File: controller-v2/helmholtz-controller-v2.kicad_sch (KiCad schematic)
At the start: 25 parts, among them U1 BDS63150AFM, U2 BDS63150AFM, U3 INA226, U4 INA226, U5 BDS63150AFM, U6 INA226, U7 RPi_Pico

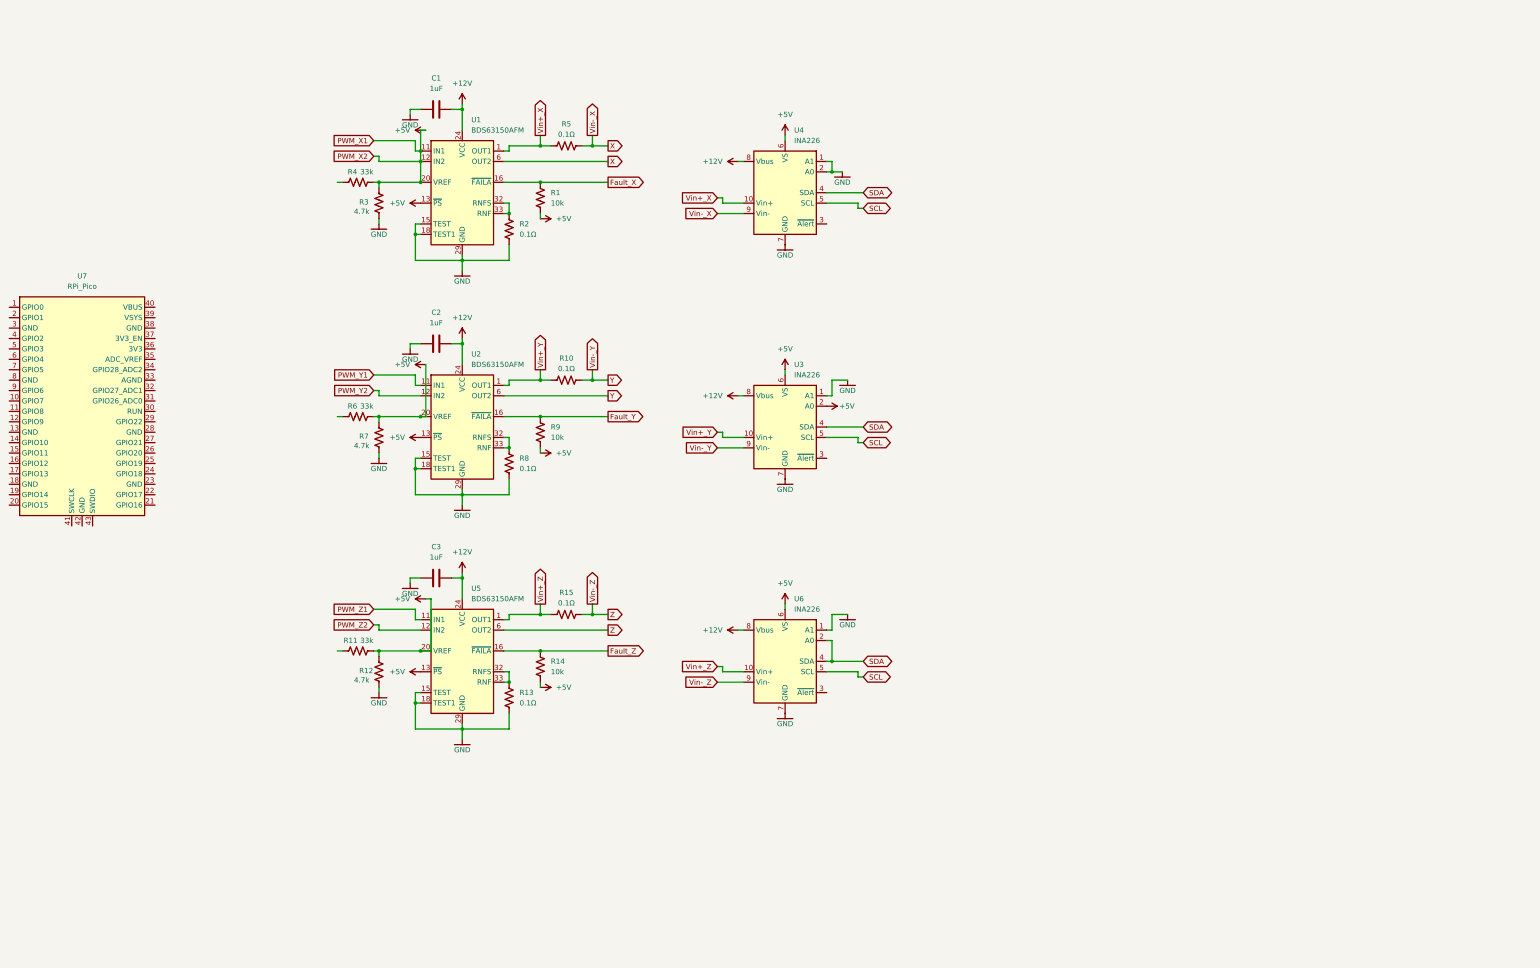
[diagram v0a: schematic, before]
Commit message: Improved schematic, made it more readable
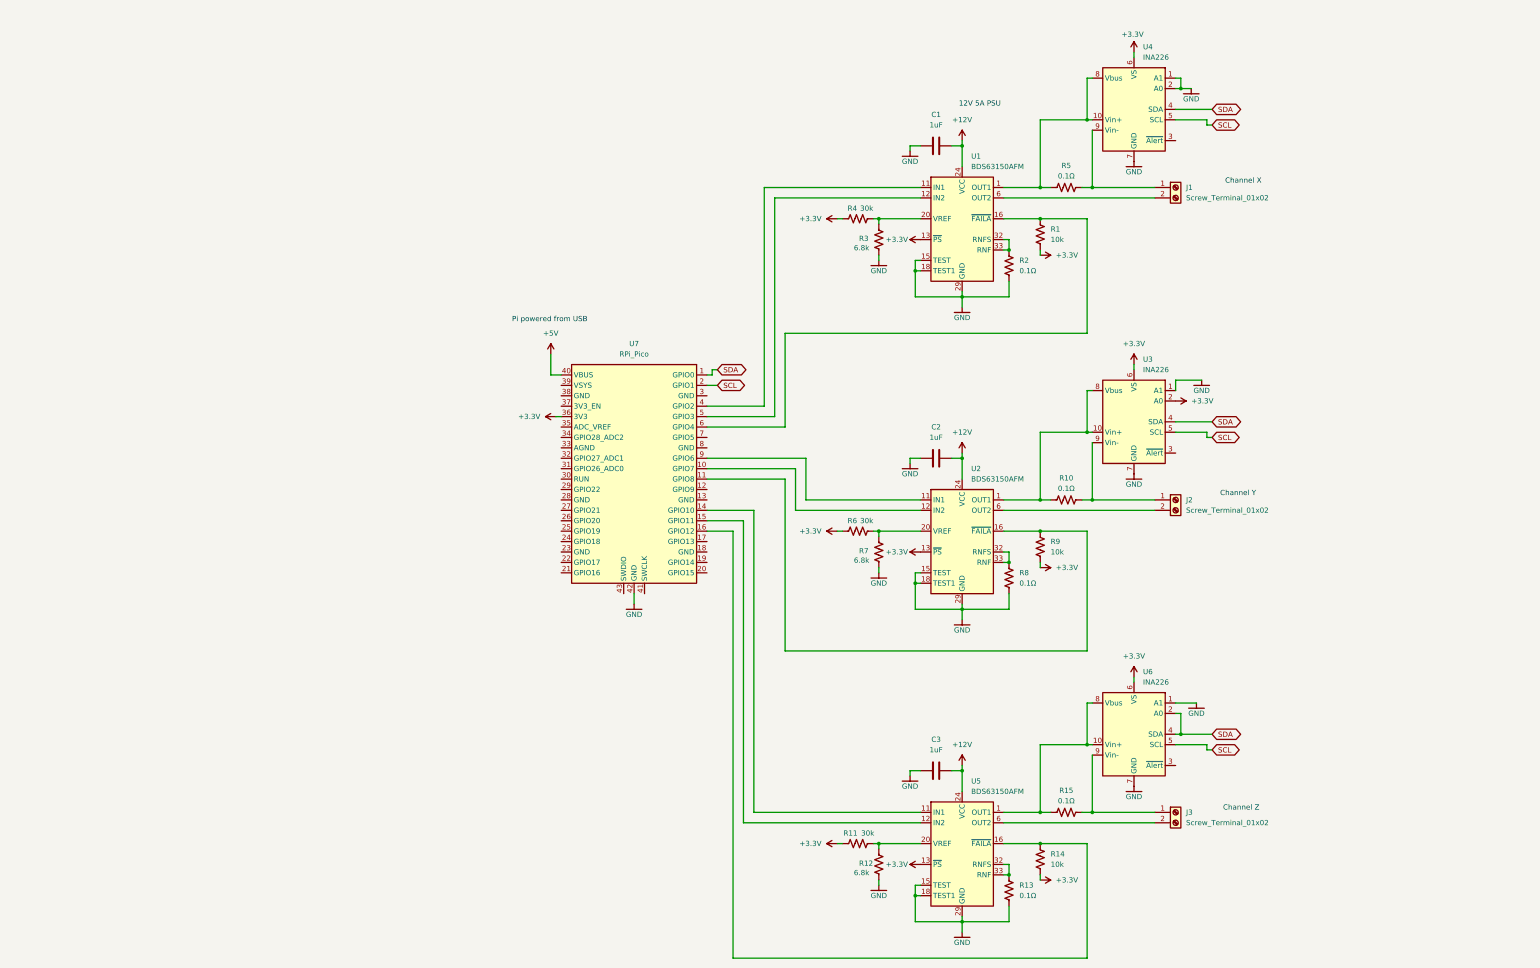
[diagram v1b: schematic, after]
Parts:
- added J1, J2, J3: Screw_Terminal_01x02, symbol Connector:Screw_Terminal_01x02
- R11, R4, R6: value 33k -> 30k
- R12, R3, R7: value 4.7k -> 6.8k
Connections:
- net Fault_X is gone; now on an unnamed net: R1.1, U1.16 (~{FAILA})
- net Fault_Y is gone; now on an unnamed net: R9.1, U2.16 (~{FAILA})
- net Fault_Z is gone; now on an unnamed net: R14.1, U5.16 (~{FAILA})
- net PWM_Y1 is gone; now on an unnamed net: U2.11 (IN1)
- net PWM_Y2 is gone; now on an unnamed net: U2.12 (IN2)
- net PWM_Z1 is gone; now on an unnamed net: U5.11 (IN1)
- net PWM_Z2 is gone; now on an unnamed net: U5.12 (IN2)
- net +12V: no longer U3.8 (Vbus), U4.8 (Vbus), U6.8 (Vbus)
- net +5V: now also U7.40 (VBUS); no longer R1.2, R11.2, R12.2, R14.2, R3.2, R4.2, R6.2, R7.2, R9.2, U1.11 (IN1), U1.12 (IN2), U1.13 (~{PS}), U1.20 (VREF), U2.13 (~{PS}), U2.20 (VREF), U3.2 (A0), U3.6 (VS), U4.6 (VS), U5.13 (~{PS}), U5.20 (VREF), U6.6 (VS)
- net GND: now also U7.42 (GND)
- net SCL: now also U7.2 (GPIO1)
- net SDA: now also U7.1 (GPIO0)
- net +3.3V: now reaches U7.36 (3V3)
- net +3.3V: now also R1.2, R11.1, R14.2, R4.1, R6.1, R9.2, U1.13 (~{PS}), U2.13 (~{PS}), U3.2 (A0), U3.6 (VS), U4.6 (VS), U5.13 (~{PS}), U6.6 (VS)
- net at U7.4 (GPIO2): now also U1.11 (IN1)
- net at U7.5 (GPIO3): now also U1.12 (IN2)
- net Vin+_X: no longer names the net of R5.1, U1.1 (OUT1), U1.2 (OUT1), U1.3 (OUT1), U4.10 (Vin+)
- net Vin+_X: now also U4.8 (Vbus)
- net Vin+_Y: no longer names the net of R10.1, U2.1 (OUT1), U2.2 (OUT1), U2.3 (OUT1), U3.10 (Vin+)
- net Vin+_Y: now also U3.8 (Vbus)
- net Vin+_Z: no longer names the net of R15.1, U5.1 (OUT1), U5.2 (OUT1), U5.3 (OUT1), U6.10 (Vin+)
- net Vin+_Z: now also U6.8 (Vbus)
- net Vin-_X: no longer names the net of U1.6 (OUT2), U1.7 (OUT2), U1.8 (OUT2)
- net Vin-_X: now also J1.2 (Pin_2); no longer R5.2, U4.9 (Vin-)
- net Vin-_Y: no longer names the net of U2.6 (OUT2), U2.7 (OUT2), U2.8 (OUT2)
- net Vin-_Y: now also J2.2 (Pin_2); no longer R10.2, U3.9 (Vin-)
- net Vin-_Z: no longer names the net of U5.6 (OUT2), U5.7 (OUT2), U5.8 (OUT2)
- net Vin-_Z: now also J3.2 (Pin_2); no longer R15.2, U6.9 (Vin-)
- new net: R6.2, R7.2, U2.20 (VREF)
- new net: J2.1 (Pin_1), R10.2, U3.9 (Vin-)
- new net: R11.2, R12.2, U5.20 (VREF)
- new net: J1.1 (Pin_1), R5.2, U4.9 (Vin-)
- new net: J3.1 (Pin_1), R15.2, U6.9 (Vin-)
- new net: R3.2, R4.2, U1.20 (VREF)
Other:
- note added: "12V 5A PSU"
- note added: "Channel X"
- note added: "Channel Y"
- note added: "Channel Z"
- note added: "Pi powered from USB"
- title: (none) -> Helmholtz Cage Controller
- moved on the sheet: C1, R1, R2, R3, R4, R5, U1, U4, U7

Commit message: ADded 12V connector and I2C resistors
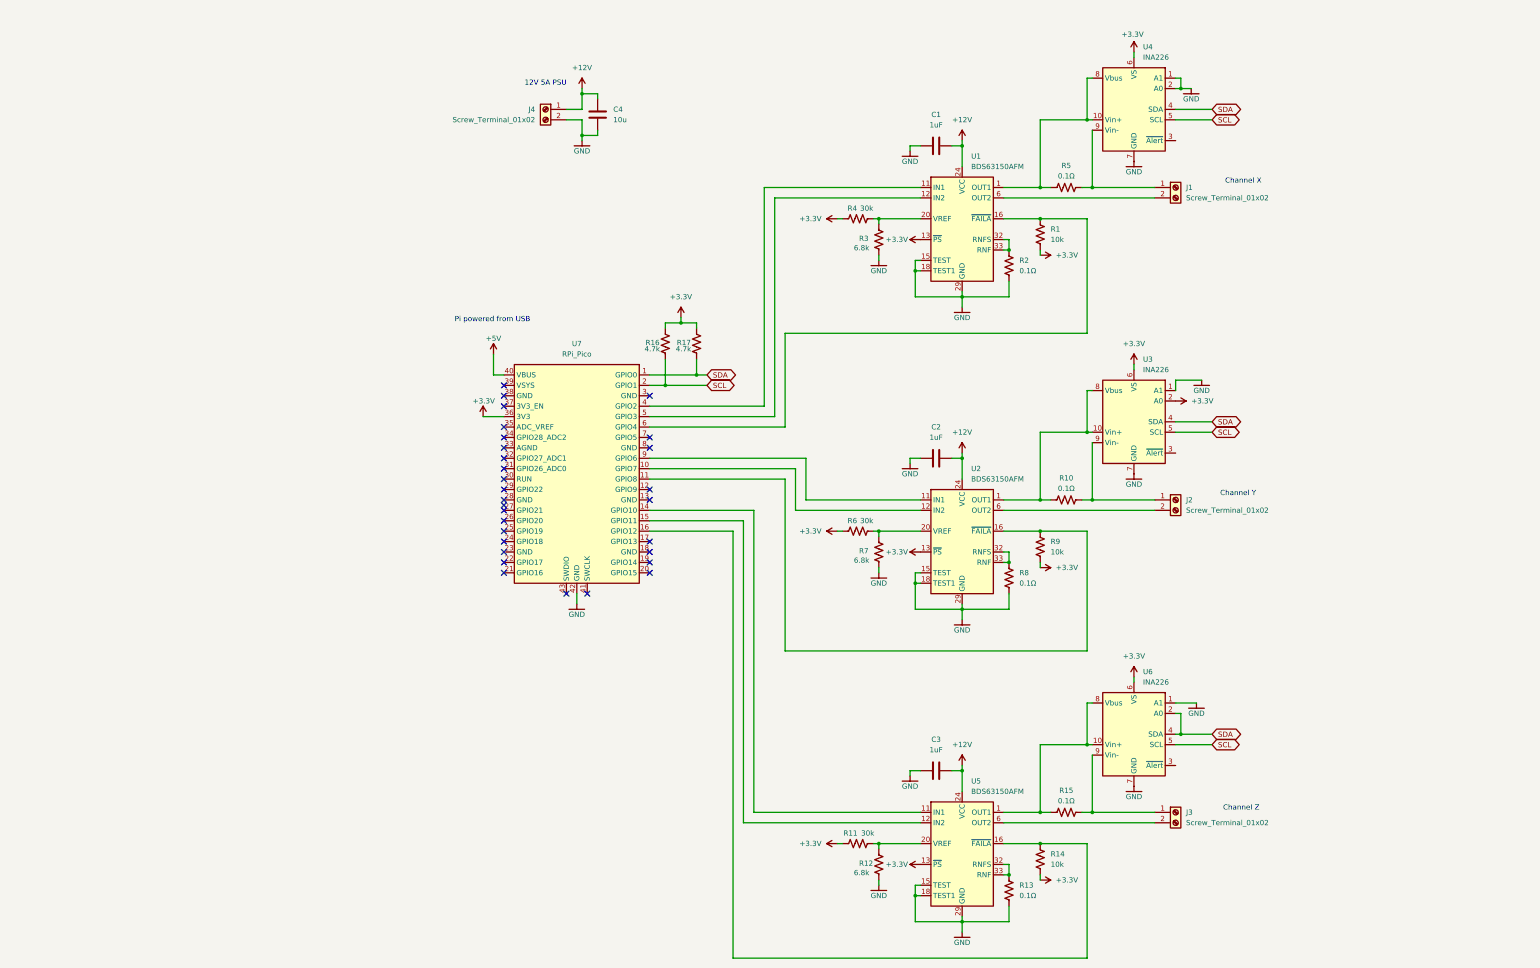
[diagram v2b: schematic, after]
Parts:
- added C4: 10u, symbol Device:C
- added J4: Screw_Terminal_01x02, symbol Connector:Screw_Terminal_01x02
- added R16, R17: 4.7k, symbol Device:R_US
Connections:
- net +12V: now also C4.2, J4.1 (Pin_1)
- net +3.3V: now also R16.2, R17.2
- net GND: now also C4.1, J4.2 (Pin_2)
- net SCL: now also R16.1
- net SDA: now also R17.1
- no-connect marks 0 -> 30
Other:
- moved on the sheet: U7

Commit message: updated schematic
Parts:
- C1, C2, C3, C4: footprint (none) -> Capacitor_SMD:C_0805_2012Metric
- J1, J2, J3, J4: footprint (none) -> TerminalBlock_Phoenix:TerminalBlock_Phoenix_PT-1,5-4-3.5-H_1x04_P3.50mm_Horizontal
- R1, R11, R12, R14, R16, R17, R3, R4, R6, R7, R9: footprint (none) -> Resistor_SMD:R_0603_1608Metric
- R10, R13, R15, R2, R5, R8: footprint (none) -> Resistor_SMD:R_1206_3216Metric
- U1, U2, U5: footprint (none) -> psas-footprints:U-BD63150AFM
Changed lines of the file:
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@@
 			)
 		)
-		(property "Footprint" ""
+		(property "Footprint" "Resistor_SMD:R_1206_3216Metric"
 			(at 234.696 155.194 90)
 			(effects
@@
 			)
 		)
-		(property "Footprint" ""
+		(property "Footprint" "Resistor_SMD:R_0603_1608Metric"
 			(at 197.104 142.494 90)
 			(effects
@@
 			)
 		)
-		(property "Footprint" ""
+		(property "Footprint" "Resistor_SMD:R_0603_1608Metric"
 			(at 156.464 97.536 90)
 			(effects
@@
 			)
 		)
-		(property "Footprint" ""
+		(property "Footprint" "psas-footprints:U-BD63150AFM"
 			(at 222.25 125.73 0)
 			(effects
@@
 			)
 		)
-		(property "Footprint" ""
+		(property "Footprint" "Capacitor_SMD:C_0805_2012Metric"
 			(at 219.71 124.7648 0)
 			(effects
@@
 			)
 		)
-		(property "Footprint" ""
+		(property "Footprint" "Resistor_SMD:R_0603_1608Metric"
 			(at 242.316 223.774 90)
 			(effects
@@
 			)
 		)
-		(property "Footprint" ""
+		(property "Footprint" "psas-footprints:U-BD63150AFM"
 			(at 222.25 201.93 0)
 			(effects
@@
 			)
 		)
-		(property "Footprint" ""
+		(property "Footprint" "TerminalBlock_Phoenix:TerminalBlock_Phoenix_PT-1,5-4-3.5-H_1x04_P3.50mm_Horizontal"
 			(at 274.32 59.69 0)
 			(effects
@@
 			)
 		)
-		(property "Footprint" ""
+		(property "Footprint" "Resistor_SMD:R_0603_1608Metric"
 			(at 200.914 224.536 90)
 			(effects
@@
 			)
 		)
-		(property "Footprint" ""
+		(property "Footprint" "Capacitor_SMD:C_0805_2012Metric"
 			(at 219.71 48.5648 0)
 			(effects
@@
 			)
 		)
-		(property "Footprint" ""
+		(property "Footprint" "TerminalBlock_Phoenix:TerminalBlock_Phoenix_PT-1,5-4-3.5-H_1x04_P3.50mm_Horizontal"
 			(at 274.32 212.09 0)
 			(effects
@@
 			)
 		)
-		(property "Footprint" ""
+		(property "Footprint" "Resistor_SMD:R_1206_3216Metric"
 			(at 234.696 78.994 90)
 			(effects
@@
 			)
 		)
-		(property "Footprint" ""
+		(property "Footprint" "Capacitor_SMD:C_0805_2012Metric"
 			(at 132.3848 38.1 0)
 			(effects
@@
 			)
 		)
-		(property "Footprint" ""
+		(property "Footprint" "Resistor_SMD:R_0603_1608Metric"
 			(at 242.316 71.374 90)
 			(effects
@@
 			)
 		)
-		(property "Footprint" ""
+		(property "Footprint" "TerminalBlock_Phoenix:TerminalBlock_Phoenix_PT-1,5-4-3.5-H_1x04_P3.50mm_Horizontal"
 			(at 120.65 40.64 0)
 			(effects
@@
 			)
 		)
-		(property "Footprint" ""
+		(property "Footprint" "Resistor_SMD:R_1206_3216Metric"
 			(at 234.696 231.394 90)
 			(effects
@@
 			)
 		)
-		(property "Footprint" ""
+		(property "Footprint" "Resistor_SMD:R_0603_1608Metric"
 			(at 242.316 147.574 90)
 			(effects
@@
 			)
 		)
-		(property "Footprint" ""
+		(property "Footprint" "Resistor_SMD:R_1206_3216Metric"
 			(at 247.904 58.674 90)
 			(effects
@@
 			)
 		)
-		(property "Footprint" ""
+		(property "Footprint" "Resistor_SMD:R_0603_1608Metric"
 			(at 197.104 218.694 90)
 			(effects
@@
 			)
 		)
-		(property "Footprint" ""
+		(property "Footprint" "Resistor_SMD:R_1206_3216Metric"
 			(at 247.904 211.074 90)
 			(effects
@@
 			)
 		)
-		(property "Footprint" ""
+		(property "Footprint" "TerminalBlock_Phoenix:TerminalBlock_Phoenix_PT-1,5-4-3.5-H_1x04_P3.50mm_Horizontal"
 			(at 274.32 135.89 0)
 			(effects
@@
 			)
 		)
-		(property "Footprint" ""
+		(property "Footprint" "Capacitor_SMD:C_0805_2012Metric"
 			(at 219.71 200.9648 0)
 			(effects
@@
 			)
 		)
-		(property "Footprint" ""
+		(property "Footprint" "Resistor_SMD:R_0603_1608Metric"
 			(at 200.914 148.336 90)
 			(effects
@@
 			)
 		)
-		(property "Footprint" ""
+		(property "Footprint" "Resistor_SMD:R_0603_1608Metric"
 			(at 197.104 66.294 90)
 			(effects
@@
 			)
 		)
-		(property "Footprint" ""
+		(property "Footprint" "psas-footprints:U-BD63150AFM"
 			(at 222.25 49.53 0)
 			(effects
@@
 			)
 		)
-		(property "Footprint" ""
+		(property "Footprint" "Resistor_SMD:R_0603_1608Metric"
 			(at 200.914 72.136 90)
 			(effects
@@
 			)
 		)
-		(property "Footprint" ""
+		(property "Footprint" "Resistor_SMD:R_1206_3216Metric"
 			(at 247.904 134.874 90)
 			(effects
@@
 			)
 		)
-		(property "Footprint" ""
+		(property "Footprint" "Resistor_SMD:R_0603_1608Metric"
 			(at 148.844 97.536 90)
 			(effects

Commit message: Updated schematic & board
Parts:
- added C5, C6, C7: 1uF, Capacitor_SMD:C_0805_2012Metric, symbol Device:C
- J1, J2, J3, J4: footprint TerminalBlock_Phoenix:TerminalBlock_Phoenix_PT-1,5-4-3.5-H_1x04_P3.50mm_Horizontal -> TerminalBlock_Phoenix:TerminalBlock_Phoenix_PT-1,5-2-3.5-H_1x02_P3.50mm_Horizontal
- R10, R13, R15, R2, R5, R8: value 0.1Ω -> 100m
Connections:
- net +3.3V: now also R1.1, C5.2, C6.2, C7.2; no longer R1.2
- net GND: now also C5.1, C6.1, C7.1
- net at U1.16 (~{FAILA}), U7.6 (GPIO4): now also R1.2; no longer R1.1
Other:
- note added: "addr: 0x80"
- note added: "addr:0x81"
- note added: "addr:0x82"
- moved on the sheet: R1, R14, R9
